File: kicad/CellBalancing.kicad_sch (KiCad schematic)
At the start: 150 parts, among them U15 ETA3000, U16 ETA3000, U18 ETA3000, U19 ETA3000, U22 ETA3000, U23 ETA3000, U25 ETA3000, U26 ETA3000, U28 ETA3000, U29 ETA3000, U31 ETA3000, U32 ETA3000, U33 ETA3000, U34 ETA3000, U35 ETA3000

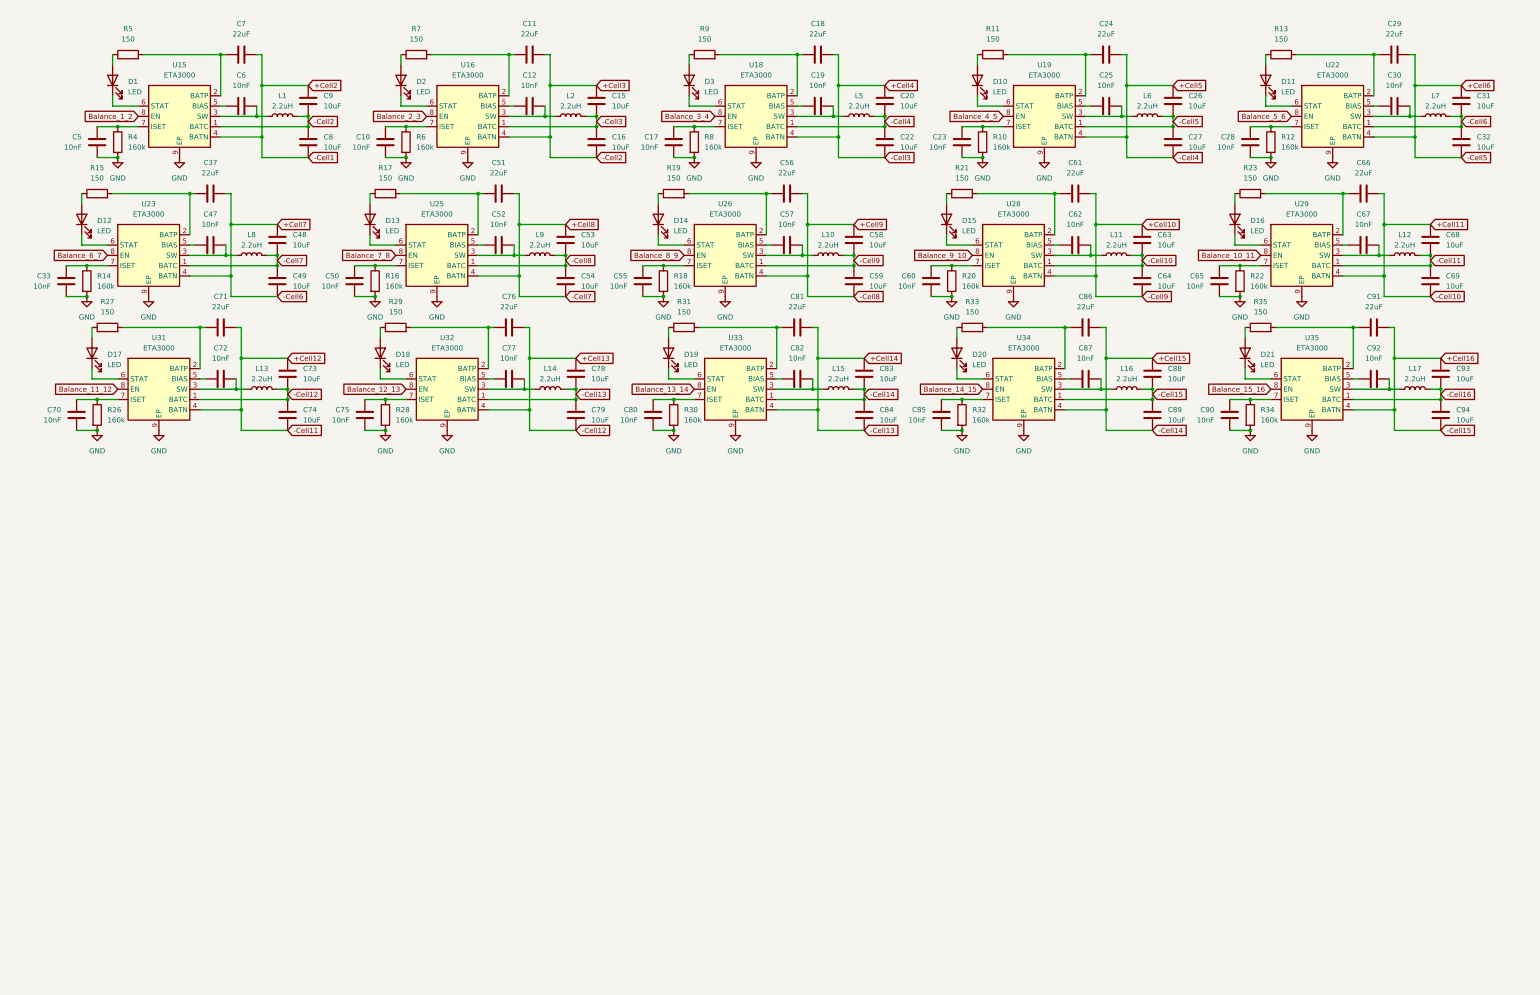
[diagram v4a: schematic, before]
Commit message: made full cell balancing up to 36S
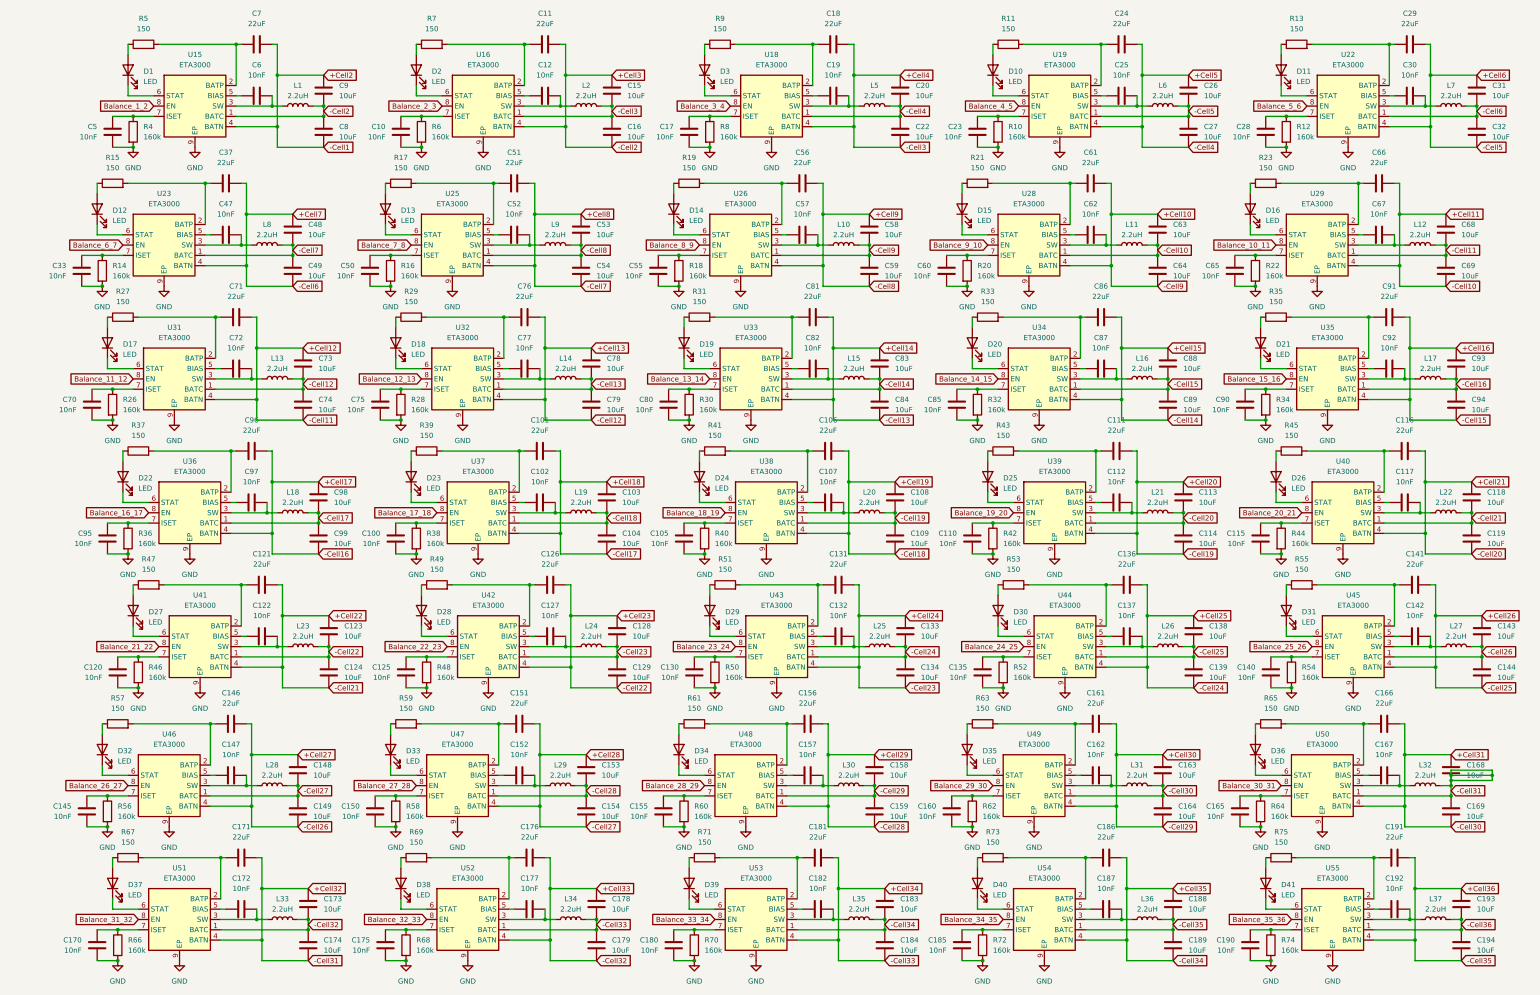
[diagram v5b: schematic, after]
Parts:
- added C100, C102, C105, C107, C110, C112, C115, C117, C120, C122, C125, C127, C130, C132, C135, C137, C140, C142, C145, C147, C150, C152, C155, C157, C160, C162, C165, C167, C170, C172, C175, C177, C180, C182, C185, C187, C190, C192, C95, C97: 10nF, symbol Device:C
- added C101, C106, C111, C116, C121, C126, C131, C136, C141, C146, C151, C156, C161, C166, C171, C176, C181, C186, C191, C96: 22uF, symbol Device:C
- added C103, C104, C108, C109, C113, C114, C118, C119, C123, C124, C128, C129, C133, C134, C138, C139, C143, C144, C148, C149, C153, C154, C158, C159, C163, C164, C168, C169, C173, C174, C178, C179, C183, C184, C188, C189, C193, C194, C98, C99: 10uF, symbol Device:C
- added D22, D23, D24, D25, D26, D27, D28, D29, D30, D31, D32, D33, D34, D35, D36, D37, D38, D39, D40, D41: LED, symbol Device:LED
- added L18, L19, L20, L21, L22, L23, L24, L25, L26, L27, L28, L29, L30, L31, L32, L33, L34, L35, L36, L37: 2.2uH, symbol Device:L
- added R36, R38, R40, R42, R44, R46, R48, R50, R52, R54, R56, R58, R60, R62, R64, R66, R68, R70, R72, R74: 160k, symbol Device:R
- added R37, R39, R41, R43, R45, R47, R49, R51, R53, R55, R57, R59, R61, R63, R65, R67, R69, R71, R73, R75: 150, symbol Device:R
- added U36, U37, U38, U39, U40, U41, U42, U43, U44, U45, U46, U47, U48, U49, U50, U51, U52, U53, U54, U55: ETA3000, Package_DFN_QFN:DFN-8-1EP_2x2mm_P0.5mm_EP0.9x1.3mm, symbol Battery_Management:ETA3000
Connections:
- net GND: now also C100.2, C105.2, C110.2, C115.2, C120.2, C125.2, C130.2, C135.2, C140.2, C145.2, C150.2, C155.2, C160.2, C165.2, C170.2, C175.2, C180.2, C185.2, C190.2, C95.2, R36.2, R38.2, R40.2, R42.2, R44.2, R46.2, R48.2, R50.2, R52.2, R54.2, R56.2, R58.2, R60.2, R62.2, R64.2, R66.2, R68.2, R70.2, R72.2, R74.2, U36.9 (EP), U37.9 (EP), U38.9 (EP), U39.9 (EP), U40.9 (EP), U41.9 (EP), U42.9 (EP), U43.9 (EP), U44.9 (EP), U45.9 (EP), U46.9 (EP), U47.9 (EP), U48.9 (EP), U49.9 (EP), U50.9 (EP), U51.9 (EP), U52.9 (EP), U53.9 (EP), U54.9 (EP), U55.9 (EP)
- net -Cell16 renamed +Cell17
- net +Cell17: now also C96.2, C98.1, C99.2, U36.4 (BATN)
- new net: D22.1 (K), U36.6 (STAT)
- new net: D22.2 (A), R37.1
- new net: C157.1, U48.5 (BIAS)
- new net: C157.2, L30.1, U48.3 (SW)
- new net: D35.2 (A), R63.1
- new net: C161.1, R63.2, U49.2 (BATP)
- new net: C101.1, R39.2, U37.2 (BATP)
- new net: C102.2, L19.1, U37.3 (SW)
- new net: C102.1, U37.5 (BIAS)
- new net: D23.1 (K), U37.6 (STAT)
- new net: C100.1, R38.1, U37.7 (ISET)
- new net: C182.2, L35.1, U53.3 (SW)
- new net: C152.2, L29.1, U47.3 (SW)
- new net: C111.1, R43.2, U39.2 (BATP)
- new net: C177.2, L34.1, U52.3 (SW)
- new net: C97.1, U36.5 (BIAS)
- new net: C97.2, L18.1, U36.3 (SW)
- new net: D29.1 (K), U43.6 (STAT)
- new net: D29.2 (A), R51.1
- new net: C125.1, R48.1, U42.7 (ISET)
- new net: C132.1, U43.5 (BIAS)
- new net: C132.2, L25.1, U43.3 (SW)
- new net: C171.1, R67.2, U51.2 (BATP)
- new net: C172.2, L33.1, U51.3 (SW)
- new net: C172.1, U51.5 (BIAS)
- new net: D37.1 (K), U51.6 (STAT)
- new net: C170.1, R66.1, U51.7 (ISET)
- new net: C165.1, R64.1, U50.7 (ISET)
- new net: C175.1, R68.1, U52.7 (ISET)
- new net: C96.1, R37.2, U36.2 (BATP)
- new net: C160.1, R62.1, U49.7 (ISET)
- new net: D40.2 (A), R73.1
- new net: C186.1, R73.2, U54.2 (BATP)
- new net: C187.2, L36.1, U54.3 (SW)
- new net: C187.1, U54.5 (BIAS)
- new net: D40.1 (K), U54.6 (STAT)
- new net: C185.1, R72.1, U54.7 (ISET)
- new net: C142.2, L27.1, U45.3 (SW)
- new net: D26.2 (A), R45.1
- new net: C116.1, R45.2, U40.2 (BATP)
- new net: D33.2 (A), R59.1
- new net: C151.1, R59.2, U47.2 (BATP)
- new net: D35.1 (K), U49.6 (STAT)
- new net: C155.1, R60.1, U48.7 (ISET)
- new net: D23.2 (A), R39.1
- new net: D39.2 (A), R71.1
- new net: C181.1, R71.2, U53.2 (BATP)
- new net: C135.1, R52.1, U44.7 (ISET)
- new net: C150.1, R58.1, U47.7 (ISET)
- new net: C136.1, R53.2, U44.2 (BATP)
- new net: C137.2, L26.1, U44.3 (SW)
- new net: C137.1, U44.5 (BIAS)
- new net: D30.1 (K), U44.6 (STAT)
- new net: C140.1, R54.1, U45.7 (ISET)
- new net: C167.1, U50.5 (BIAS)
- new net: C167.2, L32.1, U50.3 (SW)
- new net: D24.1 (K), U38.6 (STAT)
- new net: D24.2 (A), R41.1
- new net: C176.1, R69.2, U52.2 (BATP)
- new net: D38.2 (A), R69.1
- new net: C122.1, U41.5 (BIAS)
- new net: C122.2, L23.1, U41.3 (SW)
- new net: C110.1, R42.1, U39.7 (ISET)
- new net: D31.1 (K), U45.6 (STAT)
- new net: D31.2 (A), R55.1
- new net: C141.1, R55.2, U45.2 (BATP)
- new net: C162.2, L31.1, U49.3 (SW)
- new net: C95.1, R36.1, U36.7 (ISET)
- new net: D28.2 (A), R49.1
- new net: C126.1, R49.2, U42.2 (BATP)
- new net: D41.1 (K), U55.6 (STAT)
- new net: D41.2 (A), R75.1
- new net: C112.2, L21.1, U39.3 (SW)
- new net: C112.1, U39.5 (BIAS)
- new net: D25.1 (K), U39.6 (STAT)
- new net: C131.1, R51.2, U43.2 (BATP)
- new net: C180.1, R70.1, U53.7 (ISET)
- new net: C162.1, U49.5 (BIAS)
- new net: C152.1, U47.5 (BIAS)
- new net: D36.1 (K), U50.6 (STAT)
- new net: D36.2 (A), R65.1
- new net: D34.2 (A), R61.1
- new net: C156.1, R61.2, U48.2 (BATP)
- new net: C191.1, R75.2, U55.2 (BATP)
- new net: C192.2, L37.1, U55.3 (SW)
- new net: C192.1, U55.5 (BIAS)
- new net: C190.1, R74.1, U55.7 (ISET)
- new net: D37.2 (A), R67.1
- new net: C177.1, U52.5 (BIAS)
- new net: C105.1, R40.1, U38.7 (ISET)
- new net: D39.1 (K), U53.6 (STAT)
- new net: C130.1, R50.1, U43.7 (ISET)
- new net: C145.1, R56.1, U46.7 (ISET)
- new net: C147.1, U46.5 (BIAS)
- new net: C147.2, L28.1, U46.3 (SW)
- new net: C106.1, R41.2, U38.2 (BATP)
- new net: D33.1 (K), U47.6 (STAT)
- new net: C107.1, U38.5 (BIAS)
- new net: C107.2, L20.1, U38.3 (SW)
- new net: C115.1, R44.1, U40.7 (ISET)
- new net: D25.2 (A), R43.1
- new net: D27.1 (K), U41.6 (STAT)
- new net: D27.2 (A), R47.1
- new net: D28.1 (K), U42.6 (STAT)
- new net: C146.1, R57.2, U46.2 (BATP)
- new net: D32.1 (K), U46.6 (STAT)
- new net: C166.1, R65.2, U50.2 (BATP)
- new net: C120.1, R46.1, U41.7 (ISET)
- new net: D32.2 (A), R57.1
- new net: C121.1, R47.2, U41.2 (BATP)
- new net: C142.1, U45.5 (BIAS)
- new net: D26.1 (K), U40.6 (STAT)
- new net: C127.2, L24.1, U42.3 (SW)
- new net: C127.1, U42.5 (BIAS)
- new net: D30.2 (A), R53.1
- new net: D34.1 (K), U48.6 (STAT)
- new net: C117.2, L22.1, U40.3 (SW)
- new net: C117.1, U40.5 (BIAS)
- new net: D38.1 (K), U52.6 (STAT)
- new net: C182.1, U53.5 (BIAS)
- new net +Cell18: C101.2, C103.1, C104.2, C98.2, C99.1, L18.2, U36.1 (BATC), U37.4 (BATN)
- new net +Cell19: C103.2, C104.1, C106.2, C108.1, C109.2, L19.2, U37.1 (BATC), U38.4 (BATN)
- new net +Cell20: C108.2, C109.1, C111.2, C113.1, C114.2, L20.2, U38.1 (BATC), U39.4 (BATN)
- new net +Cell21: C113.2, C114.1, C116.2, C118.1, C119.2, L21.2, U39.1 (BATC), U40.4 (BATN)
- new net +Cell22: C118.2, C119.1, C121.2, C123.1, C124.2, L22.2, U40.1 (BATC), U41.4 (BATN)
- new net +Cell23: C123.2, C124.1, C126.2, C128.1, C129.2, L23.2, U41.1 (BATC), U42.4 (BATN)
- new net +Cell24: C128.2, C129.1, C131.2, C133.1, C134.2, L24.2, U42.1 (BATC), U43.4 (BATN)
- new net +Cell25: C133.2, C134.1, C136.2, C138.1, C139.2, L25.2, U43.1 (BATC), U44.4 (BATN)
- new net +Cell26: C138.2, C139.1, C141.2, C143.1, C144.2, L26.2, U44.1 (BATC), U45.4 (BATN)
- new net +Cell27: C143.2, C144.1, C146.2, C148.1, C149.2, L27.2, U45.1 (BATC), U46.4 (BATN)
- new net +Cell28: C148.2, C149.1, C151.2, C153.1, C154.2, L28.2, U46.1 (BATC), U47.4 (BATN)
- new net +Cell29: C153.2, C154.1, C156.2, C158.1, C159.2, L29.2, U47.1 (BATC), U48.4 (BATN)
- new net +Cell30: C158.2, C159.1, C161.2, C163.1, C164.2, L30.2, U48.1 (BATC), U49.4 (BATN)
- new net +Cell31: C163.2, C164.1, C166.2, C168.1, C169.2, L31.2, U49.1 (BATC), U50.4 (BATN)
- new net +Cell32: C168.2, C169.1, C171.2, C173.1, C174.2, L32.2, U50.1 (BATC), U51.4 (BATN)
- new net +Cell33: C173.2, C174.1, C176.2, C178.1, C179.2, L33.2, U51.1 (BATC), U52.4 (BATN)
- new net +Cell34: C178.2, C179.1, C181.2, C183.1, C184.2, L34.2, U52.1 (BATC), U53.4 (BATN)
- new net +Cell35: C183.2, C184.1, C186.2, C188.1, C189.2, L35.2, U53.1 (BATC), U54.4 (BATN)
- new net +Cell36: C188.2, C189.1, C191.2, C193.1, C194.2, L36.2, U54.1 (BATC), U55.4 (BATN)
- new net -Cell36: C193.2, C194.1, L37.2, U55.1 (BATC)
- new net Balance_16_17: U36.8 (EN)
- new net Balance_17_18: U37.8 (EN)
- new net Balance_18_19: U38.8 (EN)
- new net Balance_19_20: U39.8 (EN)
- new net Balance_20_21: U40.8 (EN)
- new net Balance_21_22: U41.8 (EN)
- new net Balance_22_23: U42.8 (EN)
- new net Balance_23_24: U43.8 (EN)
- new net Balance_24_25: U44.8 (EN)
- new net Balance_25_26: U45.8 (EN)
- new net Balance_26_27: U46.8 (EN)
- new net Balance_27_28: U47.8 (EN)
- new net Balance_28_29: U48.8 (EN)
- new net Balance_29_30: U49.8 (EN)
- new net Balance_30_31: U50.8 (EN)
- new net Balance_31_32: U51.8 (EN)
- new net Balance_32_33: U52.8 (EN)
- new net Balance_33_34: U53.8 (EN)
- new net Balance_34_35: U54.8 (EN)
- new net Balance_35_36: U55.8 (EN)
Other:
- moved on the sheet: C10, C11, C12, C15, C16, C17, C18, C19, C20, C22, C23, C24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

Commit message: Replaced STM32G0B1RBTx with STM32G0B1KCUx, simplified balancing control
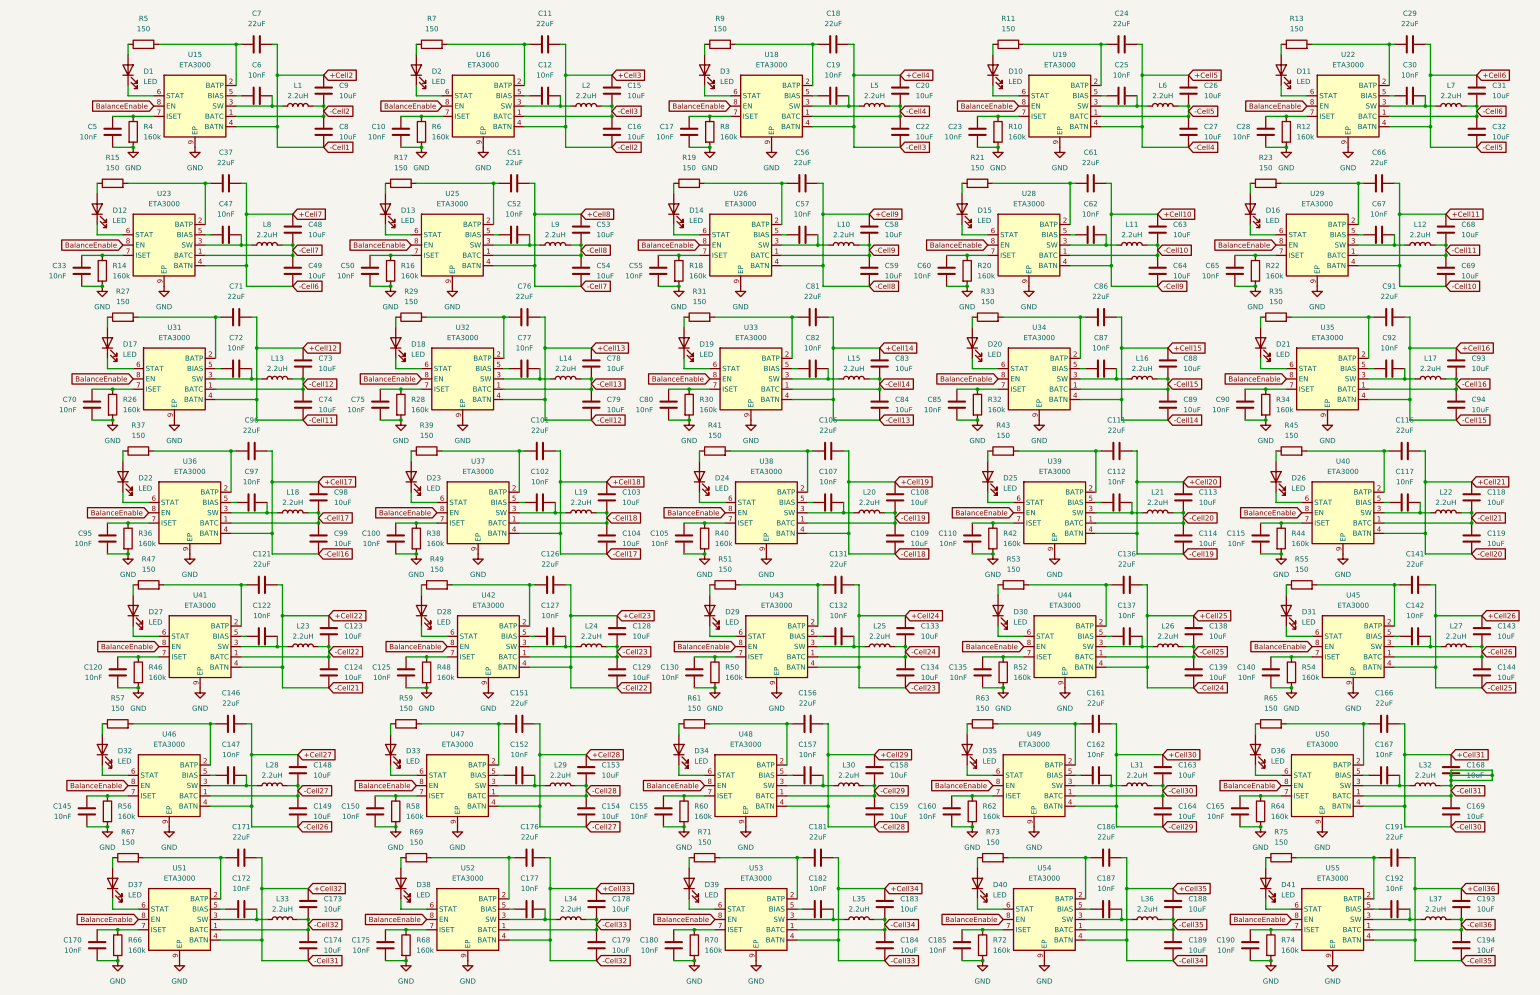
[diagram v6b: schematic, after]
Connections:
- net Balance_11_12 is gone; now on net BalanceEnable: U31.8 (EN)
- net Balance_12_13 is gone; now on net BalanceEnable: U32.8 (EN)
- net Balance_13_14 is gone; now on net BalanceEnable: U33.8 (EN)
- net Balance_14_15 is gone; now on net BalanceEnable: U34.8 (EN)
- net Balance_15_16 is gone; now on net BalanceEnable: U35.8 (EN)
- net Balance_16_17 is gone; now on net BalanceEnable: U36.8 (EN)
- net Balance_17_18 is gone; now on net BalanceEnable: U37.8 (EN)
- net Balance_18_19 is gone; now on net BalanceEnable: U38.8 (EN)
- net Balance_19_20 is gone; now on net BalanceEnable: U39.8 (EN)
- net Balance_1_2 is gone; now on net BalanceEnable: U15.8 (EN)
- net Balance_20_21 is gone; now on net BalanceEnable: U40.8 (EN)
- net Balance_21_22 is gone; now on net BalanceEnable: U41.8 (EN)
- net Balance_22_23 is gone; now on net BalanceEnable: U42.8 (EN)
- net Balance_23_24 is gone; now on net BalanceEnable: U43.8 (EN)
- net Balance_24_25 is gone; now on net BalanceEnable: U44.8 (EN)
- net Balance_25_26 is gone; now on net BalanceEnable: U45.8 (EN)
- net Balance_26_27 is gone; now on net BalanceEnable: U46.8 (EN)
- net Balance_27_28 is gone; now on net BalanceEnable: U47.8 (EN)
- net Balance_28_29 is gone; now on net BalanceEnable: U48.8 (EN)
- net Balance_29_30 is gone; now on net BalanceEnable: U49.8 (EN)
- net Balance_2_3 is gone; now on net BalanceEnable: U16.8 (EN)
- net Balance_30_31 is gone; now on net BalanceEnable: U50.8 (EN)
- net Balance_31_32 is gone; now on net BalanceEnable: U51.8 (EN)
- net Balance_32_33 is gone; now on net BalanceEnable: U52.8 (EN)
- net Balance_33_34 is gone; now on net BalanceEnable: U53.8 (EN)
- net Balance_34_35 is gone; now on net BalanceEnable: U54.8 (EN)
- net Balance_35_36 is gone; now on net BalanceEnable: U55.8 (EN)
- net Balance_3_4 is gone; now on net BalanceEnable: U18.8 (EN)
- net Balance_4_5 is gone; now on net BalanceEnable: U19.8 (EN)
- net Balance_5_6 is gone; now on net BalanceEnable: U22.8 (EN)
- net Balance_6_7 is gone; now on net BalanceEnable: U23.8 (EN)
- net Balance_7_8 is gone; now on net BalanceEnable: U25.8 (EN)
- net Balance_8_9 is gone; now on net BalanceEnable: U26.8 (EN)
- net Balance_9_10 is gone; now on net BalanceEnable: U28.8 (EN)
- net Balance_10_11 renamed BalanceEnable
